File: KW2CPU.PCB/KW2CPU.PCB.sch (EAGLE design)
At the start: 25 parts, among them IC1 AT45DB161D8S1

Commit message: LasCon, KW2 Frontend
Exported LasCon for Jeff, made "wide" version for milling test.
Schematic for KW2 front end in progress, missing F and ant connector.
Updated KW2 and GW libs with frontend parts
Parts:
- added C$10, C$9, L$6, R$4, R$5, R$7, R$8: (no value), GW-devices:RF-L
- added C$13, C$15, C$16, C$18, C$20, C$21, C$22, C$24, L$11, L$14, L$17, R$12, R$19, R$23: (no value), GW-devices:RF-C
- added U$3: RF6555, KW2:RF6555
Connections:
- new net N$19: R$7.2, U$3.RFN
- new net N$2: R$5.1, U$1.RF_OUTP
- new net N$20: R$8.2, U$3.RFP
- new net N$21: C$13.1, L$14.1, U$3.ANT1
- new net N$22: C$10.1, C$9.2, L$11.1, U$3.VCC_DIG, U$3.VCC_PA
- new net N$23: C$15.1, L$14.2
- new net N$24: C$18.1, L$17.2, U$3.ANT2
- new net N$25: C$16.1, L$17.1
- new net N$26: R$19.2, U$1.ANT_A
- new net N$27: C$20.2, R$19.1, U$3.ANTSEL
- new net N$29: R$12.1, U$3.C_LNA
- new net N$3: R$4.1, U$1.RF_OUTN
- new net N$30: C$24.1, R$23.1, U$1.RX_SWITCH, U$3.CE
- new net N$31: C$22.2, U$1.TX_SWITCH, U$3.C_RX_TX
- new net N$4: L$6.2, R$4.2, R$7.1
- new net N$5: L$6.1, R$5.2, R$8.1
- net +3V3: now also C$21.1, L$11.2, U$3.VCC_LNA
- net GND: now also C$10.2, C$13.2, C$15.2, C$16.2, C$18.2, C$20.1, C$21.2, C$22.1, C$24.2, C$9.1, R$12.2, U$3.GND, U$3.GND1, U$3.GND10, U$3.GND3, U$3.GND4, U$3.GND5, U$3.GND6, U$3.GND7, U$3.GND8, U$3.GND9

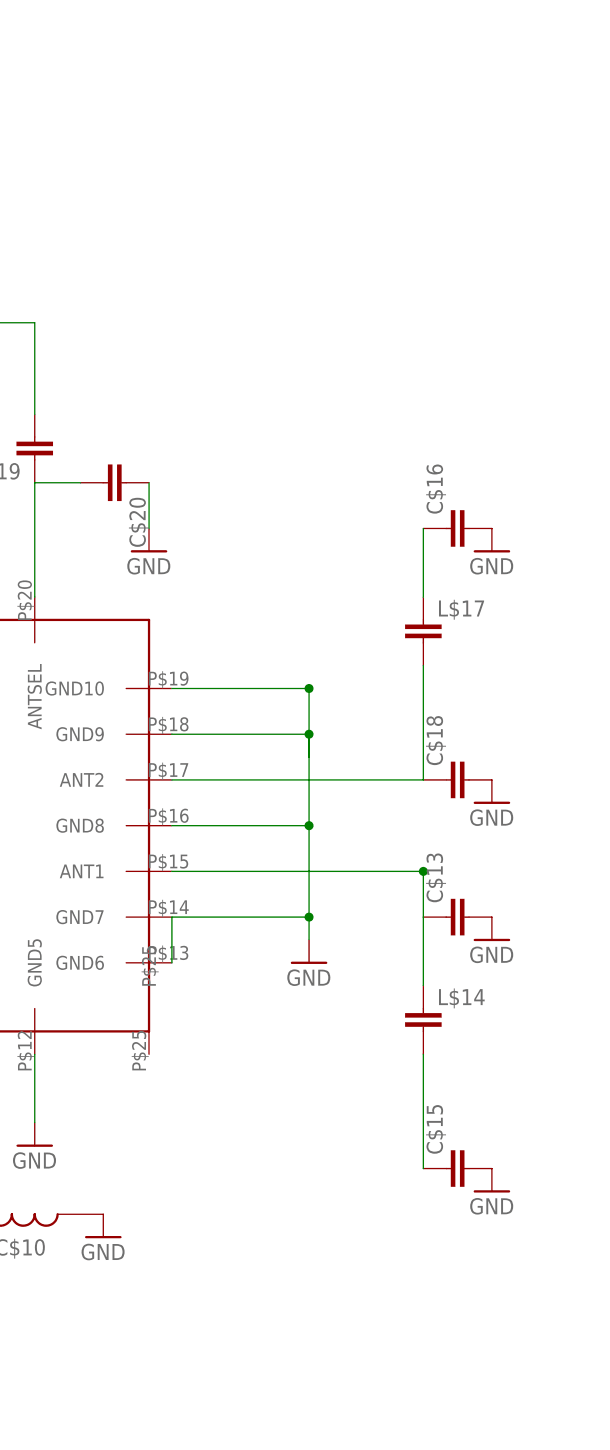
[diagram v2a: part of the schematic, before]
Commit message: KW2 antenna, LasCon panel, PosCon fiducials
Added vertical MMCX connector to KW2 design & library; added panelized
version of LasCon (old and new design); added Adafruit library and
fiducials to new PosCon
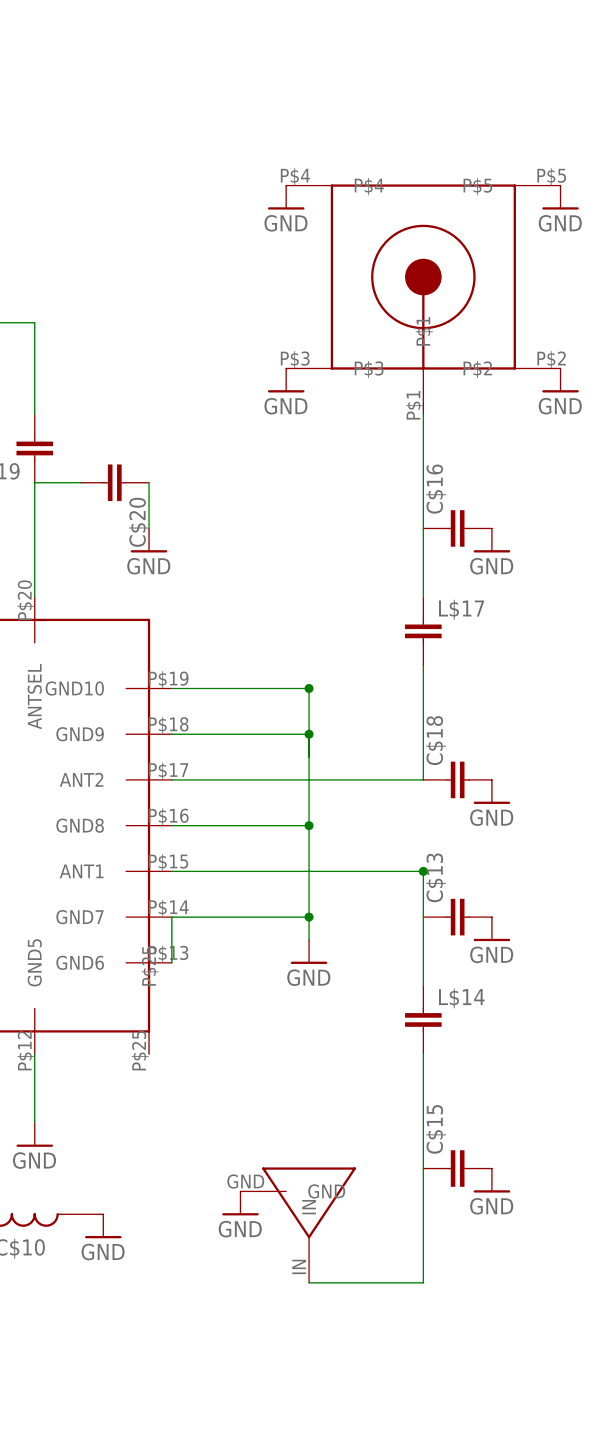
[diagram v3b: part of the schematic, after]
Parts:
- added U$4: F-ANTENNA-4LTOP, GW-devices:F-ANTENNA-4LTOP
- added U$5: MMCX_VERT, KW2:MMCX_VERT
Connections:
- net GND: now also U$4.GND, U$5.P$2, U$5.P$3, U$5.P$4, U$5.P$5
- net N$23: now also U$4.IN
- net N$25: now also U$5.P$1
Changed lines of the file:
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@@
 <part name="GND26" library="supply1" deviceset="GND" device=""/>
 <part name="GND27" library="supply1" deviceset="GND" device=""/>
+<part name="U$4" library="GW-devices" deviceset="F-ANTENNA" device="-4LTOP"/>
+<part name="GND28" library="supply1" deviceset="GND" device=""/>
+<part name="U$5" library="KW2" deviceset="MMCX_VERT" device=""/>
+<part name="GND29" library="supply1" deviceset="GND" device=""/>
+<part name="GND30" library="supply1" deviceset="GND" device=""/>
+<part name="GND31" library="supply1" deviceset="GND" device=""/>
+<part name="GND32" library="supply1" deviceset="GND" device=""/>
 </parts>
 <sheets>
@@
 <instance part="GND26" gate="1" x="157.48" y="7.62"/>
 <instance part="GND27" gate="1" x="177.8" y="-5.08"/>
+<instance part="U$4" gate="G$1" x="259.08" y="-53.34" rot="MR0"/>
+<instance part="GND28" gate="1" x="251.46" y="-50.8"/>
+<instance part="U$5" gate="G$1" x="271.78" y="53.34" rot="R90"/>
+<instance part="GND29" gate="1" x="256.54" y="40.64"/>
+<instance part="GND30" gate="1" x="287.02" y="40.64"/>
+<instance part="GND31" gate="1" x="287.02" y="60.96"/>
+<instance part="GND32" gate="1" x="256.54" y="60.96"/>
 </instances>
 <busses>
@@
 <pinref part="GND27" gate="1" pin="GND"/>
 <wire x1="193.04" y1="-2.54" x2="177.8" y2="-2.54" width="0.1524" layer="91"/>
+</segment>
+<segment>
+<pinref part="U$4" gate="G$1" pin="GND"/>
+<pinref part="GND28" gate="1" pin="GND"/>
+</segment>
+<segment>
+<pinref part="U$5" gate="G$1" pin="P$3"/>
+<pinref part="GND29" gate="1" pin="GND"/>
+</segment>
+<segment>
+<pinref part="U$5" gate="G$1" pin="P$2"/>
+<pinref part="GND30" gate="1" pin="GND"/>
+</segment>
+<segment>
+<pinref part="U$5" gate="G$1" pin="P$5"/>
+<pinref part="GND31" gate="1" pin="GND"/>
+</segment>
+<segment>
+<pinref part="U$5" gate="G$1" pin="P$4"/>
+<pinref part="GND32" gate="1" pin="GND"/>
 </segment>
 </net>
@@
 <pinref part="C$15" gate="G$1" pin="1"/>
 <wire x1="271.78" y1="-33.02" x2="271.78" y2="-45.72" width="0.1524" layer="91"/>
+<wire x1="271.78" y1="-45.72" x2="271.78" y2="-58.42" width="0.1524" layer="91"/>
+<pinref part="U$4" gate="G$1" pin="IN"/>
+<wire x1="271.78" y1="-58.42" x2="259.08" y2="-58.42" width="0.1524" layer="91"/>
 </segment>
 </net>
@@
 <pinref part="C$16" gate="G$1" pin="1"/>
 <wire x1="271.78" y1="17.78" x2="271.78" y2="25.4" width="0.1524" layer="91"/>
-</segment>
-</net>
+<pinref part="U$5" gate="G$1" pin="P$1"/>
+<wire x1="271.78" y1="25.4" x2="271.78" y2="38.1" width="0.1524" layer="91"/>
+</segment>
+</net>

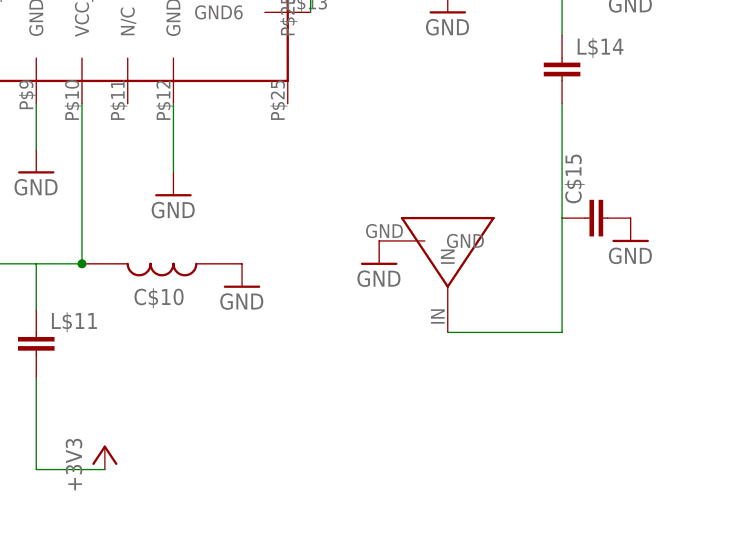
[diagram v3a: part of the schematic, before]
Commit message: PosCon parts, KW2 frontend, LasCon
Added part numbers for orange display, black buttons to PosCon. Worked
on frontend layout for KW2 and produced a new version of LasCon
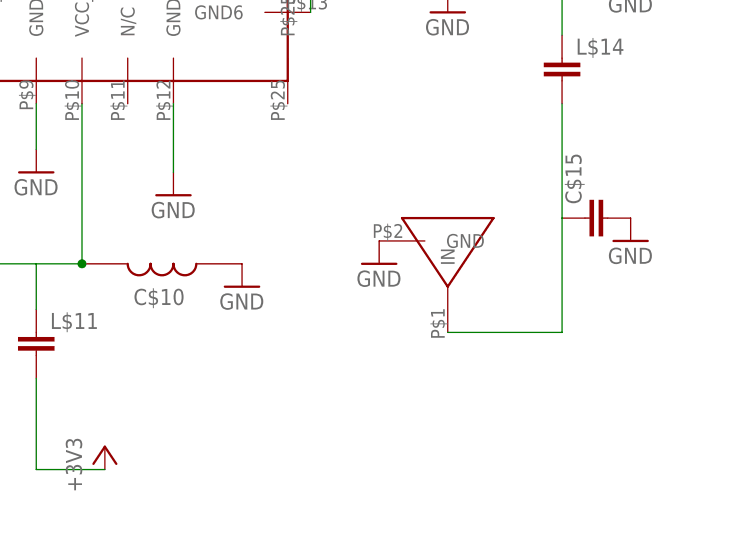
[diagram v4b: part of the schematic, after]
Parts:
- U$4: value F-ANTENNA-4LTOP -> F-ANTENNA; device GW-devices:F-ANTENNA-4LTOP -> KW2:F-ANTENNA
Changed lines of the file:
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@@
 <part name="GND26" library="supply1" deviceset="GND" device=""/>
 <part name="GND27" library="supply1" deviceset="GND" device=""/>
-<part name="U$4" library="GW-devices" deviceset="F-ANTENNA" device="-4LTOP"/>
+<part name="U$4" library="KW2" deviceset="F-ANTENNA" device=""/>
 <part name="GND28" library="supply1" deviceset="GND" device=""/>
 <part name="U$5" library="KW2" deviceset="MMCX_VERT" device=""/>

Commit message: Brain component placement
Almost finished KW2CPU component placement. Needs JTAG and memory
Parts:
- removed JP1: (no value), KW2:PINHD-2X5SMALL
- removed R$12: (no value), GW-devices:RF-C
- removed R4: 10k, GW-devices:RF-R0402
- added C3, C4: 12pF, GW-devices:RF-C0402
- added U$6: DF12_M, KW2:DF12_M
- added U$7: 32KHZ, KW2:32KHZ
- U$2: MFGN (none) -> NDK; MFGP (none) -> EXS00A-CS02368
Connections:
- removed net N$29: R$12.1, U$3.C_LNA
- new net N$28: C3.1, U$1.EXTAL32, U$7.1
- new net N$32: C4.1, U$1.XTAL32, U$7.2
- new net N$33: U$1.PTD2/LLWU_P13/SPI0_SOUT/UART2_RX/I2C0_SDA/GPIO4_BSM_DATA, U$6.P$3
- new net N$34: U$1.PTD1/ADC0_SE5B/SPI0_SCK/!UART2_CTS, U$6.P$1
- new net N$35: U$1.PTD3/SPI0_SIN/UART2_TX/I2C0_SCL/GPIO5_BSM_CLK, U$6.P$5
- new net N$36: U$1.PTD4/LLWU_P14/MADC0_SE21/SPI0_PCS1/!UART0_RTS!/FTM0_CH4/EWM_IN/GPIO_BSM_FRAME, U$6.P$7
- new net N$37: U$1.PTD5/ADC0_SE6B/SPI0_PCS2/!UART0_CTS!/!UART0_COL!/FTM0_CH5/!EWM_OUT, U$6.P$9
- new net N$38: U$1.PTD6/LLWU_P15/ADC0_SE7B/SPI0_PCS3/UART0_RX/FTM0_CH6/FTM0_FLT0, U$6.P$11
- new net N$39: U$1.PTD7/MADC0_SE22/CMT_IRO/UART0_TX/FTM0_CH7/FTM0_FLT1, U$6.P$13
- new net N$40: U$1.PTE0/MADC0_SE10/SPI1_PCS1/UART1_TX/MTRACE_CLKOUT/I2C1_SDA/RTC_CLKOUT, U$6.P$15
- new net N$41: U$1.PTE1/LLWU_P0/MADC0_SE11/SPI1_SOUT/UART1_RX/MTRACE_D3/I2C1_SCL/SPI1_SIN, U$6.P$17
- new net N$42: U$1.PTE2/LLWU_P1/MADC0_DP1/SPI1_SCK/!UART1_CTS!/MTRACE_D2, U$6.P$19
- new net N$43: U$1.PTE3/MADC0_DM1/SPI1_SIN/!UART1_RTS!/MTRACE_D1/SPI1_SOUT, U$6.P$21
- new net N$44: U$1.PTE4/LLWU_P2/SPI1_PCS0/MTRACE_D0, U$6.P$23
- new net N$45: U$1.PTE16/ADC0_SE4A/SPI0_PCS0/UART2_TX/FTM_CLKIN0/FTM0_FLT3, U$6.P$25
- new net N$46: U$1.PTE17/ADC0_SE5A/SPI0_SCK/UART2_RX/FTM_CLKIN1/LPTMR0_ALT3, U$6.P$27
- new net N$47: U$1.PTE18/ADC0_SE6A/SPI0_SOUT/!UART2_CTS!/I2C0_SDA, U$6.P$29
- new net N$48: U$1.PTE19/ADC0_SE7A/SPI0_SIN/!UART2_RTS!/I2C0_SCL, U$6.P$31
- new net N$49: U$1.PTA18/EXTAL0/FTM0_FTL2_FTM_CLKIN0, U$6.P$14
- new net N$50: U$1.PTA19/XTAL0/FTM1_FLT0/FTM_CLKIN1/LPTMR0_ALT1, U$6.P$16
- net +3V3: no longer JP1.1, R4.2
- net GND: now also C3.2, C4.2, U$3.C_LNA; no longer JP1.3, JP1.5, R$12.2
- net N$10: now also U$1.PTA0/JTAG_TCLK/SWD_CLK/EZP_CLK/!UART0_CTS/!UART0_COL/FTM0_CH5, U$6.P$4; no longer JP1.2, U$1.PTA3/JTAG_TMS/SWD_DIO/UART0_RTS/FTM0_CH0
- net N$11: now also U$1.PTA1/JTAG_TDI/EZP_DI/UART0/RX/FTM0_CH6, U$6.P$6; no longer JP1.4, U$1.PTA0/JTAG_TCLK/SWD_CLK/EZP_CLK/!UART0_CTS/!UART0_COL/FTM0_CH5
- net N$12: now also U$6.P$8; no longer JP1.6
- net N$13: now also U$1.PTA3/JTAG_TMS/SWD_DIO/UART0_RTS/FTM0_CH0, U$6.P$10; no longer JP1.8, U$1.PTA1/JTAG_TDI/EZP_DI/UART0/RX/FTM0_CH6
- net N$14: now also U$6.P$2; no longer JP1.10
- net N$15: now also U$1.PTA4/LLWU_P3/!NMI!/!EZP_CS!/FTM0_CH1, U$6.P$12; no longer JP1.9, R4.1
